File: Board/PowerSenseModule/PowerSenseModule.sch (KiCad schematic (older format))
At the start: 17 parts, among them J1 Power IO, J2 CAN IO, U1 TPS82150

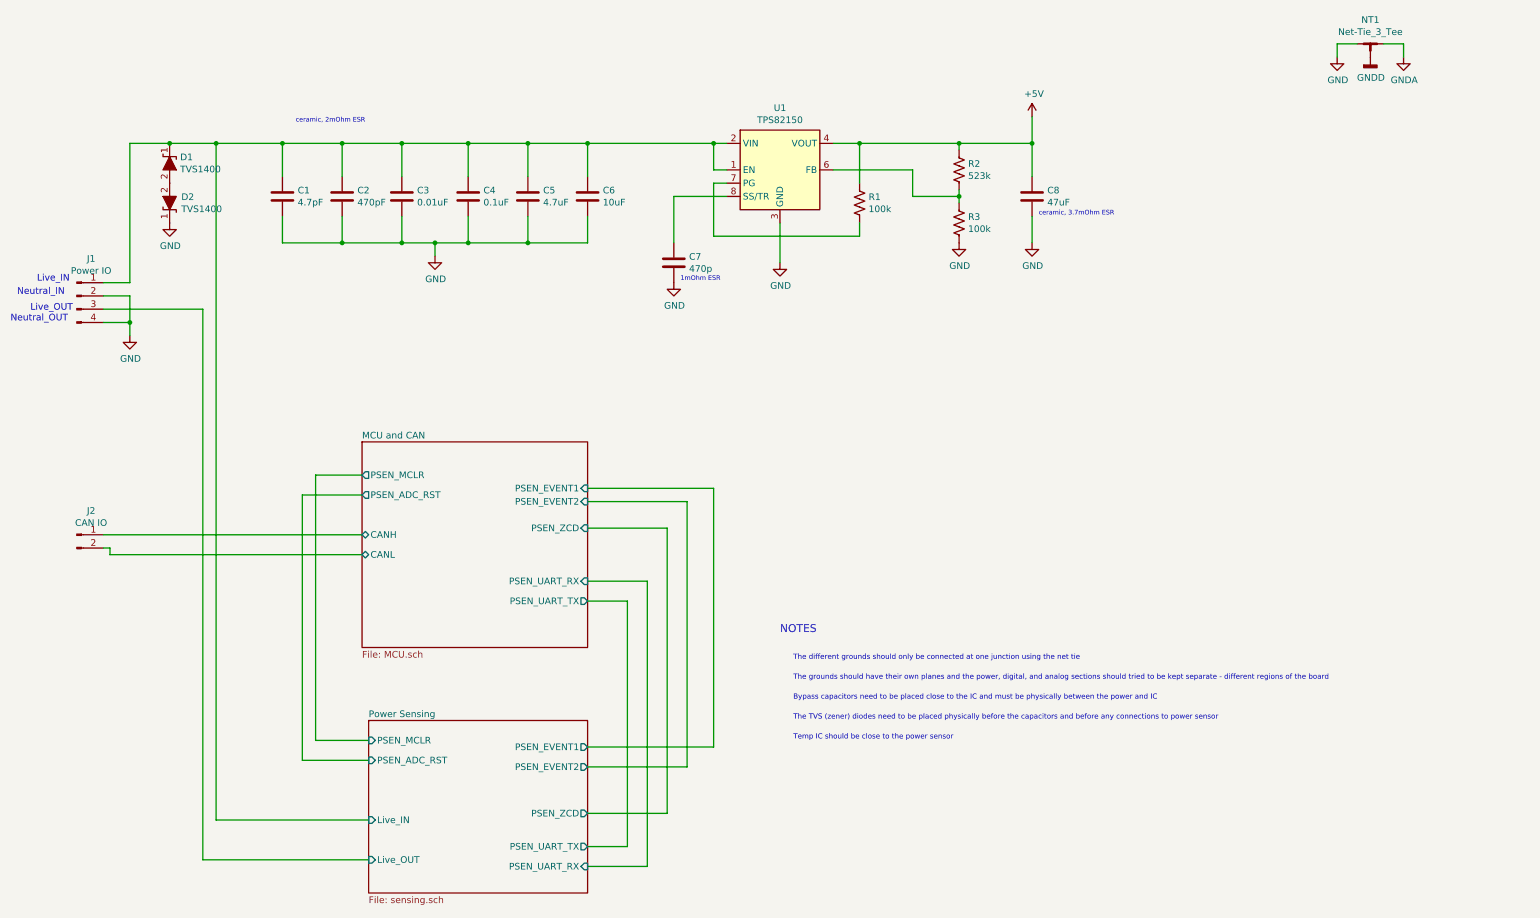
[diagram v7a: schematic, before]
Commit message: Redesign
Removed MCP power sensor for 4 op amps - buffers, differential amplifier, and active low pass, feeds into MCU adc.
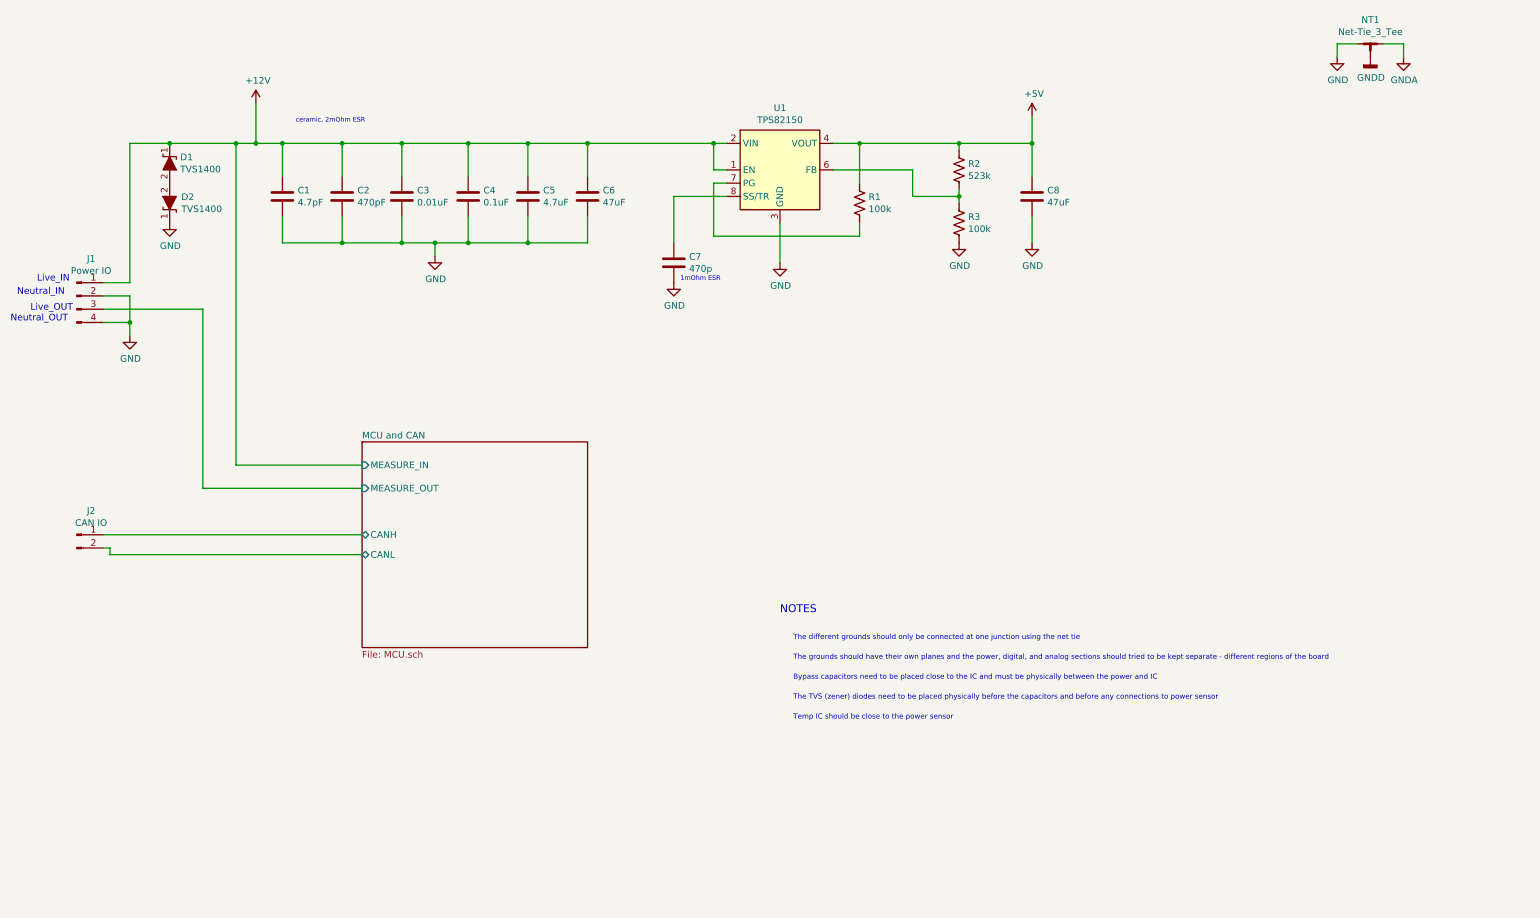
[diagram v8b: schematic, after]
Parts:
- C6: value 10uF -> 47uF
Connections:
- net Power Sensing/Live_IN renamed +12V
- net Power Sensing/Live_OUT renamed MCU and CAN/MEASURE_OUT
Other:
- note removed: "ceramic, 3.7mOhm ESR\n"
